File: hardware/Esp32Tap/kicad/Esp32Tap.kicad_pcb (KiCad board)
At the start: 4 copper layers, 95 x 58 mm, 93 parts, among them J1 430450809, J2 430451010, J3 USB-C_HRO_TYPE-C-31-M-12, K1 G6K-2F-Y-TR DC5, Q1 BC817-40,215, Q2 2N7002, SW1 SKRPACE010, SW2 SKRPACE010, U1 ESP32-S3-WROOM-1-N8, U2 TPS54202DDCR, U3 USBLC6-2SC6, U4 TPS3700DDCR, U5 TPS70950DBVR, U6 SN74LVC2G08DCTR, U7 SN74LVC1G126DBVR

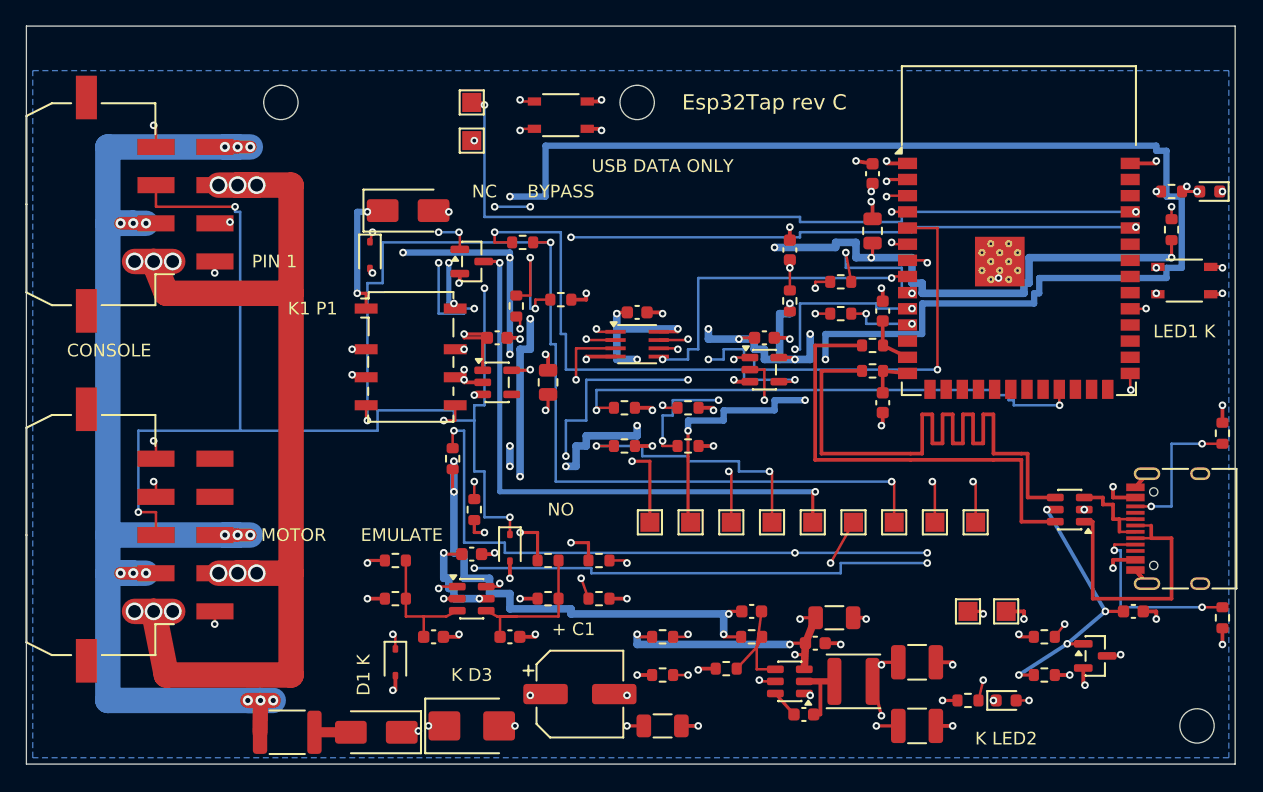
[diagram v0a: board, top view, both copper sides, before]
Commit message: hardware(Esp32Tap): add TREAD_OK series R32 + move C1 to in-stock 1210 ceramic
Two generator-driven fixes on top of the merged Rev C, both regenerated and
gate-green (make check: 744 tests, byte-reproducible artifacts, ngspice,
enclosure, fab audit, JLC stock).

- R32 (4.7k, C23162): series isolation between the TREAD_OK window-comparator
  node and ESP32 IO6. Prevents a misconfigured GPIO from overriding the U4
  voltage window or contending with its open-drain output (review finding B2).
  Splits net TREAD_OK -> TREAD_OK_MCU. Also hardens gen_pcb via_allowed() to
  check clearance on all copper layers, not just F.Cu (pre-existing latent bug).

- C1: 100uF/25V SMD electrolytic (C72477, CP_Elec_6.3x7.7) -> 22uF/25V X7R
  1210 ceramic (C2918511, same part as C6/C7). JLC had no in-stock electrolytic
  for that footprint; the ceramic is non-polarized, machine-placeable, and
  reuses an existing footprint. Reduces input bulk (acceptable: buck already
  has ceramic front-end caps); revisit value for production hold-up.

Verified on JLCPCB: all 75 parts place on Standard PCBA (J1/J2 Micro-Fit
C240838/C563827 confirmed, U1 -> N8R2 C2913204).

Note: a global lint hook black-reformatted the touched .py files, inflating the
diff; the functional change is the R32 net/part edits and the C1 part/footprint swap.

Co-Authored-By: Claude Opus 4.8 <noreply@anthropic.com>
Claude-Session: https://claude.ai/code/session_01Gopx84MbomUJwTr592YXHN
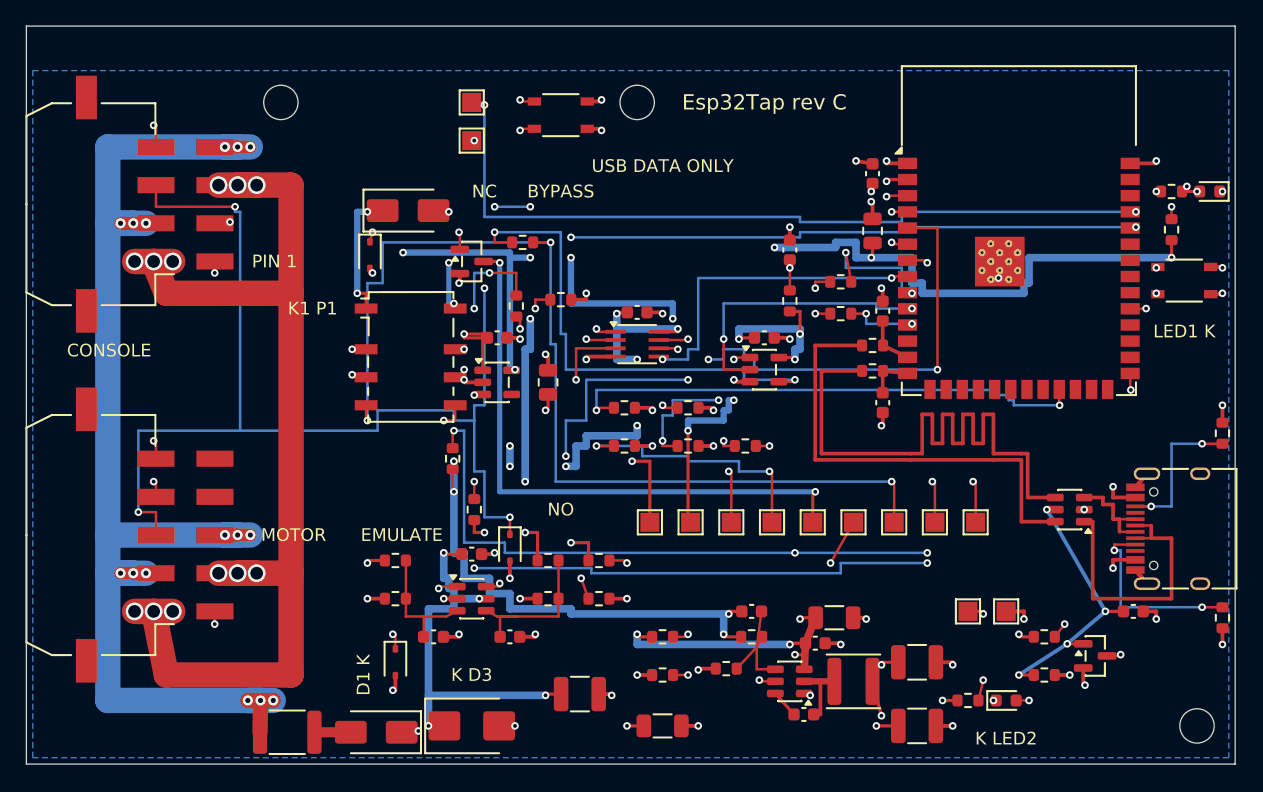
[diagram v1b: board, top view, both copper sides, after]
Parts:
- added R32: 4.7k, Resistor_SMD:R_0603_1608Metric, F.Cu at (156.5, 130.0)
- C1: value 100uF/25V -> 22uF/25V X7R 1210; footprint Capacitor_SMD:CP_Elec_6.3x7.7 -> Capacitor_SMD:C_1210_3225Metric
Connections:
- U1 pad 6: TREAD_OK -> TREAD_OK_MCU
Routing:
- net +5V_RLY: track 173.2 -> 86.4 mm, vias 11 -> 10
- net TREAD_OK_MCU: track 0.00 -> 28.1 mm, vias 0 -> 2
- net TREAD_OK: track 91.3 -> 68.4 mm
- net +3V3: track 238.4 -> 235.1 mm, vias 29 -> 27
- net Q1_B: track 27.8 -> 24.8 mm, vias 6 -> 4
- net VIN: track 159.2 -> 157.3 mm
- net ESP_TX: track 23.5 -> 22.8 mm, vias 3 -> 2
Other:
- board text removed: "+ C1"

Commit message: hardware(Esp32Tap): Rev D — on-board right-angle SMD RJ45, delete pigtails
Replace the Rev C Micro-Fit headers + external RJ45 pigtails with two
on-board, edge-mounted, right-angle SMD RJ45 jacks. Fully machine-assembled
by JLC (SMT), cheaper than Rev C, and eliminates the custom-cable line item.

- J1/J2: Molex 0441440003 (LCSC C585890) — unshielded 8P8C, right-angle,
  SMD, JLC "SMT Assembly", in stock. Edge-mounted with the mating opening
  facing off the board edge so a standard RJ45 plug reaches through the
  enclosure wall aperture. Verified right-angle by rendering the real 3D
  model (JLC's catalog "Mounting Type" field is unreliable for RJ45).
- Deleted hardware/Esp32Tap/harness/ (both pigtails, housings, terminals).
- Reused the Rev B RJ45 1:1 pinout (pin1/7 GND, 2/8 +8V, 3-6 data/serial).
- Enclosure: RJ45 wall apertures replace the Micro-Fit cutouts.
- Preserved unchanged: R32 (TREAD_OK series resistor), C1 (22uF 1210
  ceramic), ESP32-S3-N8R2, relay, buck, all other nets/parts.
- Bumped board revision C -> D (silkscreen, title block, validators, docs).

Tradeoff: the two jacks are the identical part, so the Rev C Micro-Fit
mechanical console/motor anti-swap keying is gone; CONSOLE/MOTOR silkscreen
(+ optional jack color) is the differentiator now.

make check green: 640 tests, byte-reproducible artifacts, ngspice (8 decks
x3, host+docker), enclosure validator, fab audit, JLC stock. DRC 0.

Note: a global lint hook black-reformats touched .py files, inflating the
diff; the functional change is the connector swap + harness deletion + rev bump.

Co-Authored-By: Claude Opus 4.8 (1M context) <noreply@anthropic.com>
Claude-Session: https://claude.ai/code/session_01Gopx84MbomUJwTr592YXHN
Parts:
- J1: value 430450809 -> 441440003; footprint Connector_Molex:Molex_Micro-Fit_3.0_43045-0809_2x04-1MP_P3.00mm_Horizontal -> RJ45_SMD:RJ45-SMD_441440003
- J2: value 430451010 -> 441440003; footprint Connector_Molex:Molex_Micro-Fit_3.0_43045-1010_2x05-1MP_P3.00mm_Horizontal -> RJ45_SMD:RJ45-SMD_441440003
- moved J1 6.02 mm to (108.0, 115.0)
- moved J2 4.50 mm to (108.0, 137.0)
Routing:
- net MOT6: track 38.9 -> 60.6 mm
- net +8V_RAW: track 109.5 -> 87.9 mm
- net PIN5_SAFETY: track 20.5 -> 41.9 mm
- net CONS6: track 65.2 -> 76.9 mm
- net GND: track 178.0 -> 185.9 mm
- net PIN4_PASS: track 37.7 -> 42.7 mm, vias 2 -> 3
- net PIN3: track 115.7 -> 119.4 mm
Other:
- board text added: "Esp32Tap rev D"
- board text removed: "Esp32Tap rev C"

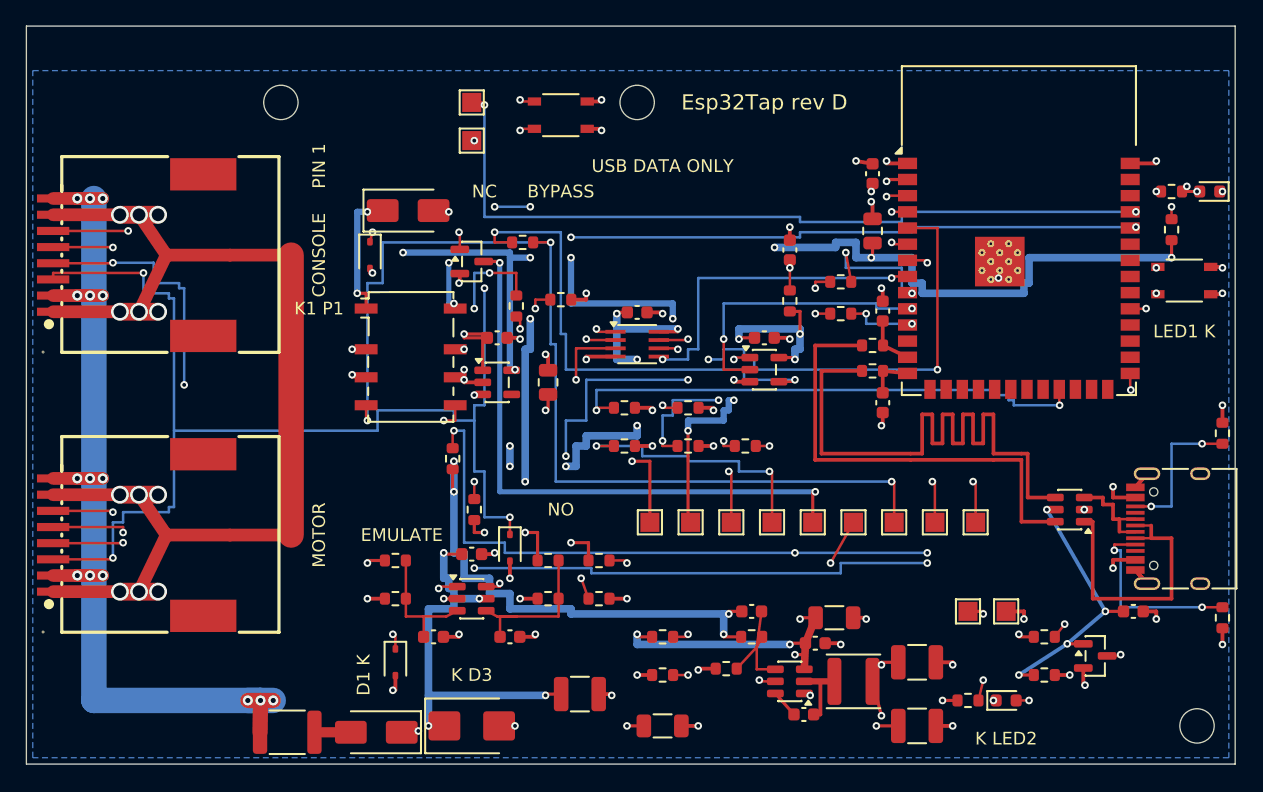
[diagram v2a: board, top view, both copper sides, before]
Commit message: hardware(Esp32Tap): Rev E layout — J2 (MOTOR) to right short edge, USB-C to bottom edge
J1 (CONSOLE) stays on the left short edge; J2 mirrors it on the right so the
board reads console-to-motor left to right. USB-C cluster (J3/U3) relocates to
the bottom edge with fully re-authored F.Cu-only matched pair (skew 0.08 mm).
Full-board +8V trunk with In1 GND mesh; router now blocks footprint-embedded
rule areas (ESP32-S3 antenna keepout) on all routing layers. All gates green:
clean-check byte-reproducible, 640 pytest, sims, DRC/ERC 0, enclosure re-cut
with one RJ45 aperture per short wall.

Known open items (next commit): RJ45 mating faces are 180° reversed (latent
Rev D bug), jacks not yet Y-aligned, silkscreen still says rev D.

Co-Authored-By: Claude Fable 5 <noreply@anthropic.com>
Claude-Session: https://claude.ai/code/session_017aRNAWKnAHt47TQVDu1G6J
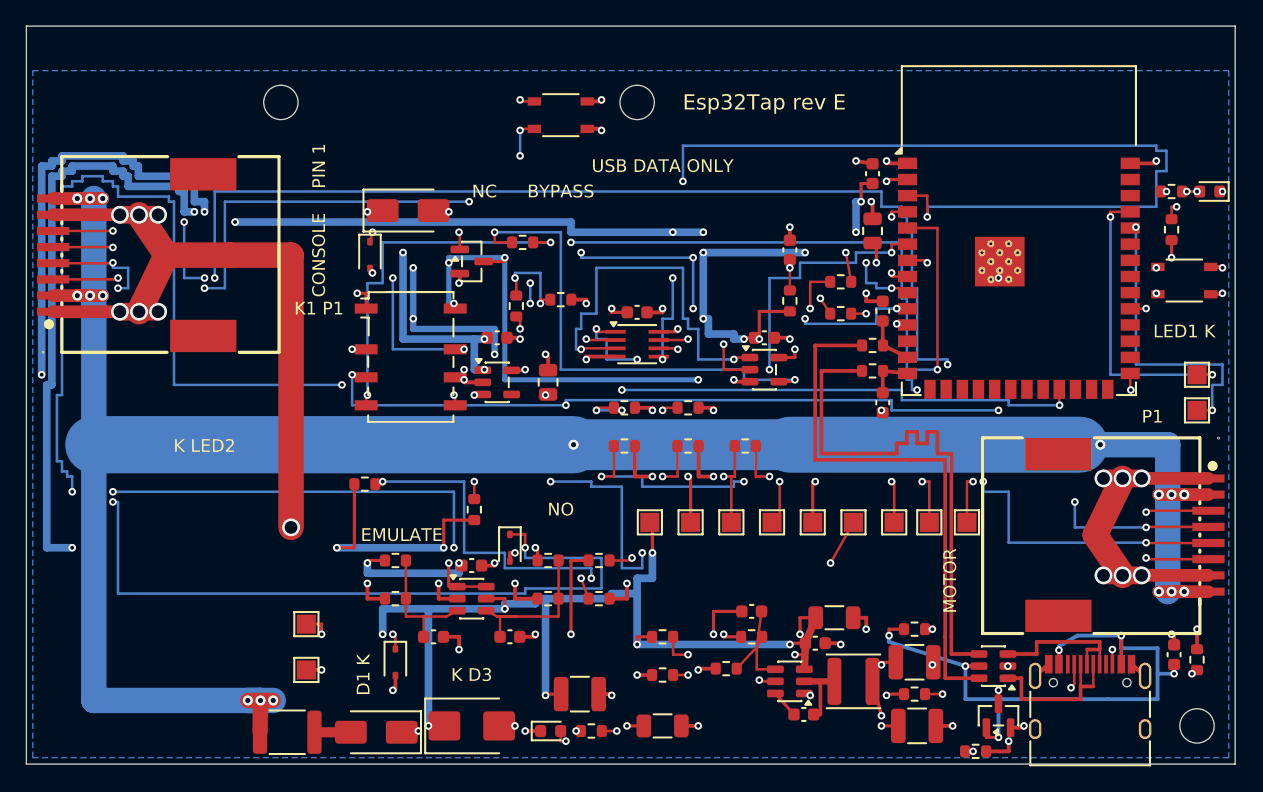
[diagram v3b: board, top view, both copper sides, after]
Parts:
- moved J2 79.0 mm to (187.0, 137.0), turned to -90 degrees
- moved TP1 60.9 mm to (192.0, 124.4)
- moved TP2 60.8 mm to (192.0, 127.2)
- moved TP4 55.2 mm to (122.0, 147.6)
- moved TP3 52.0 mm to (122.0, 144.0)
- moved LED2 35.9 mm to (141.2, 152.4)
- moved R5 31.6 mm to (174.6, 154.0), turned to 0 degrees
- moved R12 29.7 mm to (144.4, 152.4)
- moved J3 16.5 mm to (183.6, 151.2), turned to 0 degrees
- moved U3 13.7 mm to (176.0, 147.3)
- moved R30 11.1 mm to (169.8, 149.5)
- moved R29 10.8 mm to (169.8, 144.4)
- moved Q2 8.94 mm to (176.4, 151.2), turned to 90 degrees
- moved R25 7.18 mm to (126.6, 133.0), turned to 0 degrees
- moved C11 4.67 mm to (190.2, 146.4), turned to 90 degrees
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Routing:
- net GND: track 185.9 -> 661.3 mm, vias 67 -> 68
- net +8V_RAW: track 87.9 -> 290.7 mm, vias 15 -> 17
- net PIN3: track 119.4 -> 253.7 mm, vias 5 -> 10
- net +3V3: track 235.1 -> 365.0 mm, vias 27 -> 29
- net PIN4_PASS: track 42.7 -> 150.1 mm, vias 3 -> 6
- net PIN5_SAFETY: track 41.9 -> 127.7 mm, vias 2 -> 5
- net K1_NO_FB: track 129.6 -> 210.6 mm, vias 9 -> 12
- net K1_NC_FB: track 102.8 -> 180.9 mm
- net VIN: track 157.3 -> 231.6 mm, vias 16 -> 19
- net MOT6: track 60.6 -> 121.6 mm, vias 3 -> 5
- net EN: track 54.2 -> 114.5 mm, vias 4 -> 6
- net TX_GATE: track 57.4 -> 110.6 mm, vias 5 -> 6
- net U0TXD: track 62.8 -> 23.6 mm
- net U0RXD: track 61.1 -> 23.7 mm, vias 5 -> 2
- net +5V_RLY: track 86.4 -> 69.6 mm, vias 10 -> 8
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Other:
- board text added: "Esp32Tap rev E"
- board text added: "P1"
- board text removed: "Esp32Tap rev D"

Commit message: hardware(Esp32Tap): Rev E — flip RJ45s to open off-board, align both jacks at Y=37
Latent Rev D bug: the generator assumed the Molex 441440003 mating opening
faces the pad-row side (local -Y); WRL mesh analysis (port-cavity raycast,
contact-finger comb position), the Molex SD-44144-001 drawing, and the body
geometry all prove it faces local +Y. Both jacks therefore mounted 180°
backwards with ports opening into the board.

J1 (CONSOLE) now (11.9, 37.0, 270), J2 (MOTOR) (83.1, 37.0, 90): openings
off-board, body faces flush with the short edges, both jacks on one
centerline so the board reads as a straight console-to-motor passthrough.
Pad rows land 17.8 mm inboard: new under-body escape plan for J2, re-derived
J1 escapes, full power_intent entry-cluster rework (combined 2 A drop improves
97.7 -> 84.9 mV), enclosure apertures/STLs/evidence re-derived, keepout
cell-blocking gains a one-grid margin. Verified: clean-check byte-reproducible,
make check exit 0 (642 tests, ERC/DRC 0), render-inspected port direction.

Co-Authored-By: Claude Fable 5 <noreply@anthropic.com>
Claude-Session: https://claude.ai/code/session_017aRNAWKnAHt47TQVDu1G6J
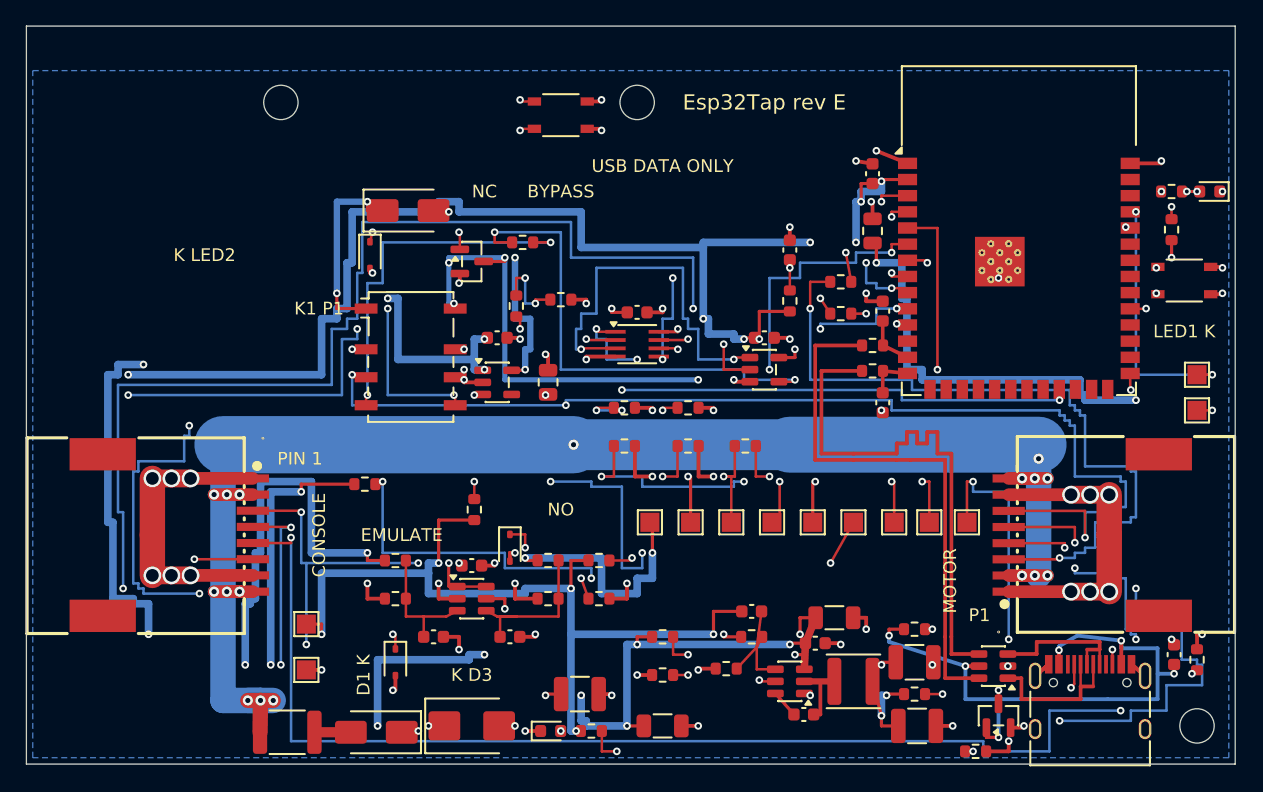
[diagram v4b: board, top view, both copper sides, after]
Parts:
- moved J1 22.3 mm to (111.9, 137.0), turned to -90 degrees
- moved J2 3.90 mm to (183.1, 137.0), turned to 90 degrees
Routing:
- net GND: track 661.3 -> 568.8 mm, vias 68 -> 67
- net +8V_RAW: track 290.7 -> 204.7 mm
- net EN: track 114.5 -> 55.8 mm, vias 6 -> 4
- net PIN3: track 253.7 -> 204.3 mm, vias 10 -> 8
- net +3V3: track 365.0 -> 332.6 mm, vias 29 -> 25
- net CONS6: track 77.5 -> 102.8 mm
- net PIN4_PASS: track 150.1 -> 126.2 mm, vias 6 -> 5
- net K1_NC_FB: track 180.9 -> 163.3 mm, vias 6 -> 7
- net VIN: track 231.6 -> 248.8 mm, vias 19 -> 22
- net PIN5_SAFETY: track 127.7 -> 118.3 mm
- net K1_NO_FB: track 210.6 -> 204.2 mm, vias 12 -> 8
- net U0TXD: track 23.6 -> 20.4 mm
- net MOT6: track 121.6 -> 124.7 mm, vias 5 -> 4
- net +5V_RLY: track 69.6 -> 67.8 mm, vias 8 -> 6
- net LED2_A: track 7.19 -> 8.79 mm
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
